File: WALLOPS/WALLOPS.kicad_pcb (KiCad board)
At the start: 2 copper layers, 55 x 67 mm, 19 parts, among them J1 JST-PH 1x8 Connector - WALLOP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, Q1 AO3401A, U1 VL53L8CX 0 (Zwicky), U2 VL58L8CX 1 (Aristotle), U3 VL53L8CX 3 (Copernicus), U4 VL53L8CX 2 (Brahe), U5 6DOF IMU (Sisko), U6 5V to 3.3V Converter

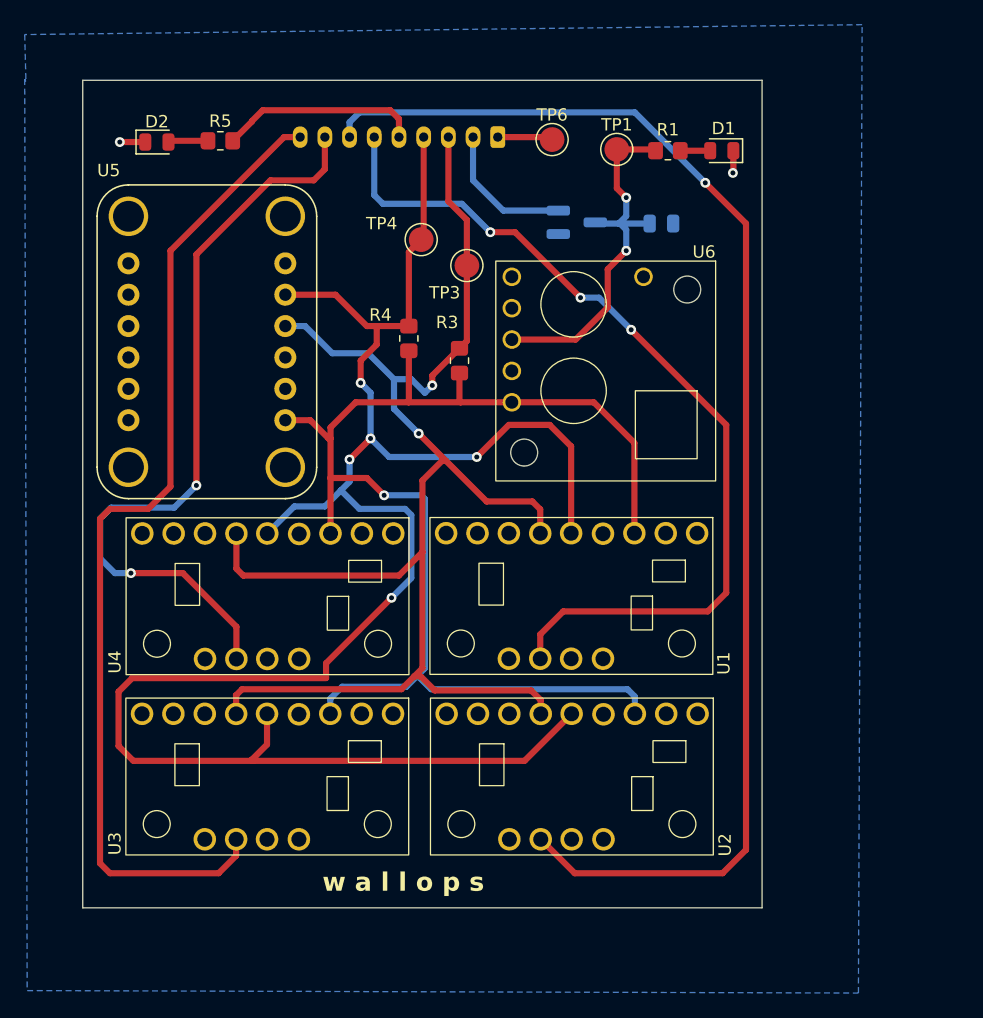
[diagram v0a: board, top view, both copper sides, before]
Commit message: Reduced size in WALLOPS
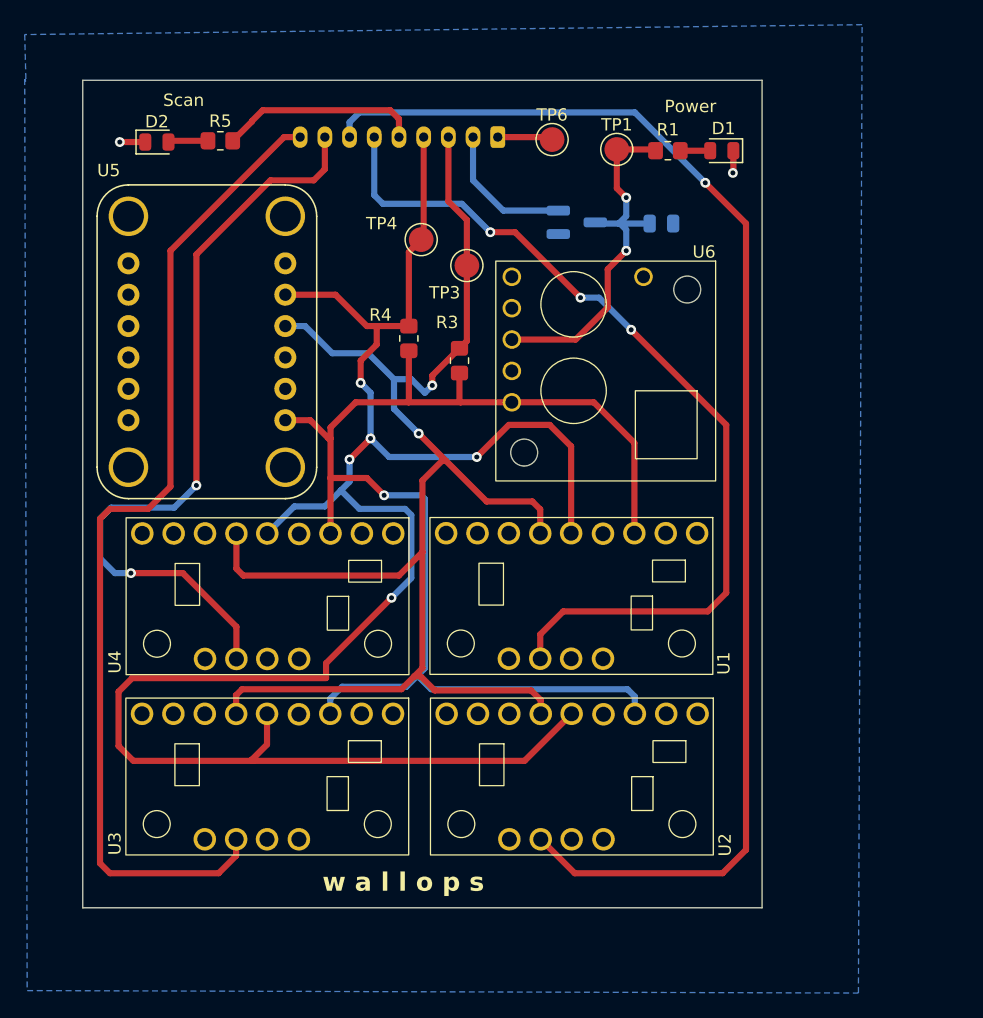
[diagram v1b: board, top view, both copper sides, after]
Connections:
- J1 pad 2: /5Vin -> /5VinML
- Q1 pad 2: /5Vin -> /5VinML
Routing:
- net /5Vin: track 42.2 -> 30.7 mm
- net /5VinML: track 0.00 -> 11.4 mm
- net /SDA: track 163.1 -> 162.5 mm
- net GND: track 8.93 -> 8.36 mm
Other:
- board text added: "Power"
- board text added: "Scan"
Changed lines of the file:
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@@
 	(net 36 "unconnected-(U6-EN-Pad2)")
 	(net 37 "unconnected-(U6-VOUT-Pad6)")
+	(net 38 "/5VinML")
 	(footprint "RockSat:VL53L8CX"
 		(layer "F.Cu")
@@
 			(layers "B.Cu" "B.Mask" "B.Paste")
 			(roundrect_rratio 0.25)
-			(net 1 "/5Vin")
+			(net 38 "/5VinML")
 			(pinfunction "S")
 			(pintype "passive")
@@
 			(layers "*.Cu" "*.Mask")
 			(remove_unused_layers no)
-			(net 1 "/5Vin")
+			(net 38 "/5VinML")
 			(pinfunction "Pin_2")
 			(pintype "passive")
@@
 		(layer "Edge.Cuts")
 	)
+	(gr_text "Scan"
+		(at 166.5 40.2 0)
+		(layer "F.SilkS")
+		(effects
+			(font
+				(size 1 1)
+				(thickness 0.15)
+			)
+			(justify left bottom)
+		)
+	)
+	(gr_text "Power"
+		(at 207.1 40.7 0)
+		(layer "F.SilkS")
+		(effects
+			(font
+				(size 1 1)
+				(thickness 0.15)
+			)
+			(justify left bottom)
+		)
+	)
 	(gr_text "w a l l o p s"
 		(at 179.4 103.8 0)
@@
 	)
 	(segment
-		(start 191.6 42.6)
-		(end 191.6 46.1)
-		(width 0.5)
-		(layer "B.Cu")
-		(net 1)
-	)
-	(segment
-		(start 204 51.8)
-		(end 204 51.9)
-		(width 0.5)
-		(layer "B.Cu")
-		(net 1)
-	)
-	(segment
-		(start 191.6 46.1)
-		(end 194.05 48.55)
-		(width 0.5)
-		(layer "B.Cu")
-		(net 1)
-	)
-	(segment
 		(start 204 50.1)
 		(end 204 51.8)
@@
 	)
 	(segment
-		(start 194.05 48.55)
-		(end 198.5 48.55)
-		(width 0.5)
-		(layer "B.Cu")
-		(net 1)
-	)
-	(segment
 		(start 201.5 49.5)
 		(end 201.7 49.5)
@@
 		(net 2)
 	)
-	(segment
-		(start 198.2 42.6)
-		(end 198.6 43)
-		(width 0.5)
-		(layer "F.Cu")
-		(net 2)
-	)
 	(via
 		(at 163 43)
@@
 	)
 	(segment
-		(start 175.4 89.77)
-		(end 174.92 89.29)
-		(width 0.5)
-		(layer "F.Cu")
-		(net 6)
-	)
-	(segment
 		(start 186.4 57.9)
 		(end 183.8 57.9)
@@
 	)
 	(segment
-		(start 163.9 77.9)
-		(end 164 77.9)
-		(width 0.5)
-		(layer "B.Cu")
-		(net 9)
-	)
-	(segment
 		(start 162.6 77.9)
 		(end 163.9 77.9)
@@
 		(net 12)
 	)
+	(segment
+		(start 191.6 42.6)
+		(end 191.6 46.1)
+		(width 0.5)
+		(layer "B.Cu")
+		(net 38)
+	)
+	(segment
+		(start 191.6 46.1)
+		(end 194.05 48.55)
+		(width 0.5)
+		(layer "B.Cu")
+		(net 38)
+	)
+	(segment
+		(start 194.05 48.55)
+		(end 198.5 48.55)
+		(width 0.5)
+		(layer "B.Cu")
+		(net 38)
+	)
 	(zone

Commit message: Updated PCB
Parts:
- removed R5: 330Ω, Resistor_SMD:R_0805_2012Metric_Pad1.20x1.40mm_HandSolder
- removed TP6: GND_TP, RockSat:TestPoint_Pad_D2.0mm_With_Tolerance
- added R2: 2.2kΩ, Resistor_SMD:R_0805_2012Metric_Pad1.20x1.40mm_HandSolder, F.Cu at (185.6, 64.7)
- added TP2: 5Vin_Test, RockSat:TestPoint_Pad_D2.0mm_With_Tolerance, F.Cu at (183.9, 59.9)
- J1: value JST-PH 1x8 Connector - WALLOPS to ML Suite -> JST-PH 1x9 Connector - WALLOPS to ML Suite; footprint Connector_JST:JST_PH_B9B-PH-K_1x09_P2.00mm_Vertical -> Connector_JST:JST_PH_S9B-PH-K_1x09_P2.00mm_Horizontal; moved to F.Cu
- R4: value 2.2kΩ -> 330Ω
- TP1: value 5Vin_Test -> GND_TP
- moved D1 44.7 mm to (167.1, 40.8)
- moved R1 44.7 mm to (162.7, 40.8)
- moved U5 34.8 mm to (204.1, 51.6)
- moved TP1 32.7 mm to (170.9, 48.7)
- moved Q1 28.6 mm to (171.7, 53.4), turned to -90 degrees
- moved C1 28.3 mm to (180.2, 59.2), turned to 90 degrees
- moved R4 27.8 mm to (162.8, 44.3), turned to 0 degrees
- moved J1 27.4 mm to (166.8, 48.7), turned to -90 degrees
- moved U6 23.2 mm to (185.1, 47.1), turned to 0 degrees
- moved TP4 19.1 mm to (175.3, 65.7)
- moved TP3 15.4 mm to (180.9, 64.6)
- moved R3 15.3 mm to (177.7, 69.0), turned to 180 degrees
- moved D2 1.89 mm to (167.3, 44.4), turned to 180 degrees
- moved U2 0.99 mm to (199.7, 93.4)
- moved U3 0.99 mm to (175.0, 93.4)
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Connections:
- R3 pad 1: /SCL -> /3.3VOUT
- R3 pad 2: /3.3VOUT -> /SDA
- R4 pad 1: /3.3VOUT -> /SCAN_LED
- R4 pad 2: /SDA -> Net-(D2-A)
- TP1 pad 1: /5Vin -> GND
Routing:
- net /SDA: track 162.5 -> 18.8 mm, vias 5 -> 0
- net /LPn_1: track 106.6 -> 0.00 mm, vias 1 -> 0
- net /LPn_3: track 81.4 -> 0.00 mm
- net /LPn_0: track 72.9 -> 0.00 mm, vias 3 -> 0
- net /LPn_2: track 62.6 -> 0.00 mm, vias 2 -> 0
- net /3.3VOUT: track 105.2 -> 64.2 mm, vias 1 -> 0
- net /SCL: track 122.2 -> 91.5 mm, vias 2 -> 3
- net /5Vin: track 30.7 -> 53.9 mm, vias 2 -> 3
- net /5VinML: track 11.4 -> 9.35 mm, vias 0 -> 1
- net GND: track 8.36 -> 9.71 mm, vias 2 -> 3
- net /SCAN_LED: track 16.3 -> 15.4 mm
- net Net-(D2-A): track 3.24 -> 2.57 mm
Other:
- outline, holes or cut-outs redrawn

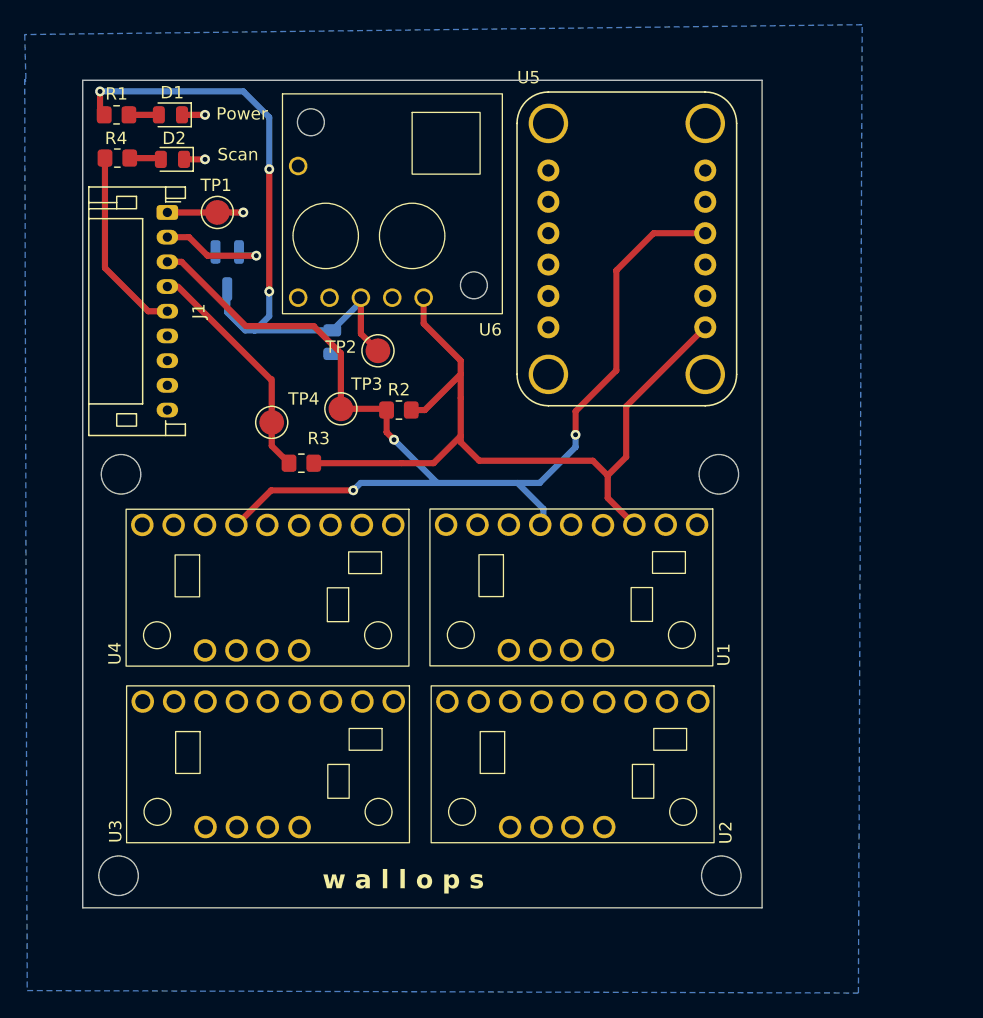
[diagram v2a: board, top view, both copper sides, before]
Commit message: Reduced size of PCB
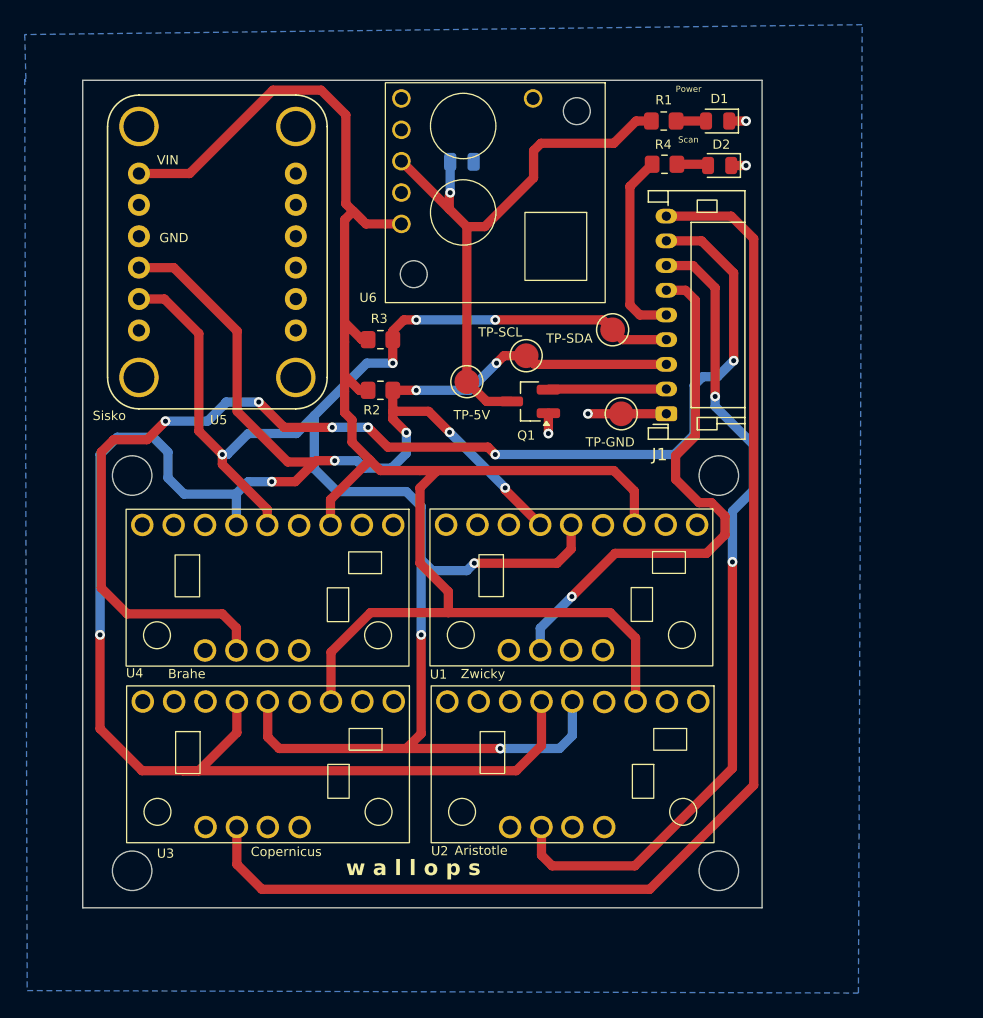
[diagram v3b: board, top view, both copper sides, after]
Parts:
- Q1: moved to F.Cu
- moved D1 44.3 mm to (211.4, 41.3)
- moved D2 44.3 mm to (211.6, 44.9)
- moved R1 44.3 mm to (207.0, 41.3)
- moved R4 44.3 mm to (207.1, 44.8)
- moved J1 43.6 mm to (207.2, 65.0), turned to 90 degrees
- moved TP-GND 36.5 mm to (203.6, 65.0), turned to -90 degrees
- moved U5 33.2 mm to (170.9, 51.9), turned to -90 degrees
- moved TP-SDA 28.6 mm to (202.9, 58.2), turned to 180 degrees
- moved Q1 26.7 mm to (196.2, 64.0), turned to 180 degrees
- moved C1 18.0 mm to (190.7, 44.6), turned to 180 degrees
- moved TP-SCL 15.6 mm to (195.9, 60.3), turned to 180 degrees
- moved R3 11.9 mm to (184.1, 59.0), turned to 0 degrees
- moved U6 9.23 mm to (194.3, 47.1), turned to -90 degrees
- moved TP-5V 7.62 mm to (191.1, 62.4), turned to 180 degrees
- moved R2 2.19 mm to (184.1, 63.1), turned to 180 degrees
- renumbered TP2 to TP-5V, TP1 to TP-GND, TP3 to TP-SCL, TP4 to TP-SDA
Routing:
- net /SDA: track 18.8 -> 147.1 mm, vias 0 -> 7
- net /LPn_3: track 0.00 -> 101.3 mm
- net /LPn_2: track 0.00 -> 98.9 mm, vias 0 -> 6
- net /SCL: track 91.5 -> 174.3 mm, vias 3 -> 8
- net /3.3VOUT: track 64.2 -> 143.6 mm
- net /LPn_1: track 0.00 -> 67.0 mm, vias 0 -> 2
- net /LPn_0: track 0.00 -> 44.5 mm, vias 0 -> 1
- net /5Vin: track 53.9 -> 48.0 mm, vias 3 -> 1
- net GND: track 9.71 -> 10.6 mm, vias 3 -> 4
- net /5VinML: track 9.35 -> 9.57 mm, vias 1 -> 0
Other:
- outline, holes or cut-outs redrawn
- board text added: "Aristotle"
- board text added: "Brahe"
- board text added: "Copernicus"
- board text added: "GND"
- board text added: "Sisko"
- board text added: "VIN"
- board text added: "Zwicky"

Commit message: Added silkscreen to WALLOPS pcb
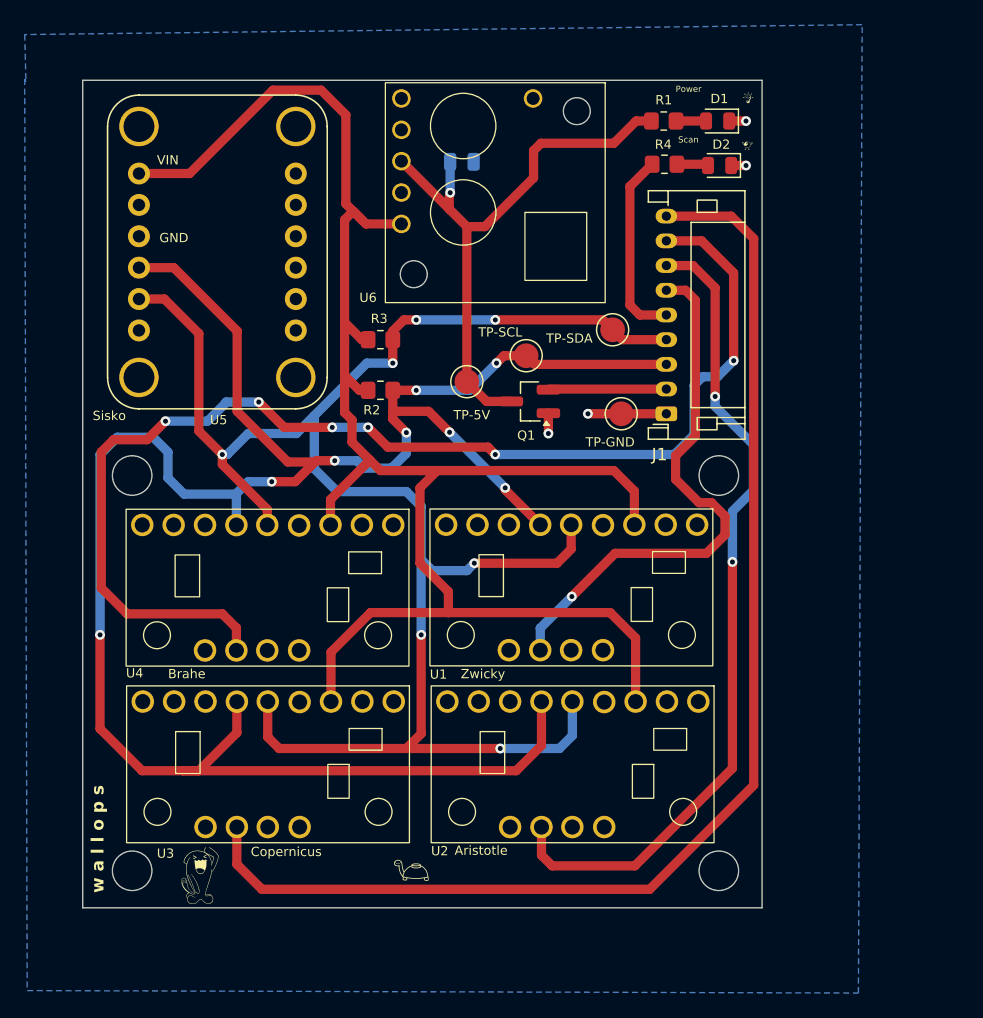
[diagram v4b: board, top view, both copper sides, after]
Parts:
- added G***: LOGO, LOGO, F.Cu at (213.9, 39.4)
- added G***: LOGO, LOGO, F.Cu at (213.8, 43.3)
- added G***: LOGO, LOGO, F.Cu at (186.7, 102.0)
- added G***: LOGO, LOGO, F.Cu at (169.5, 102.4)
- added G***: LOGO, LOGO, B.Cu at (171.0, 51.4)
- added G***: LOGO, LOGO, B.Cu at (186.1, 97.2)

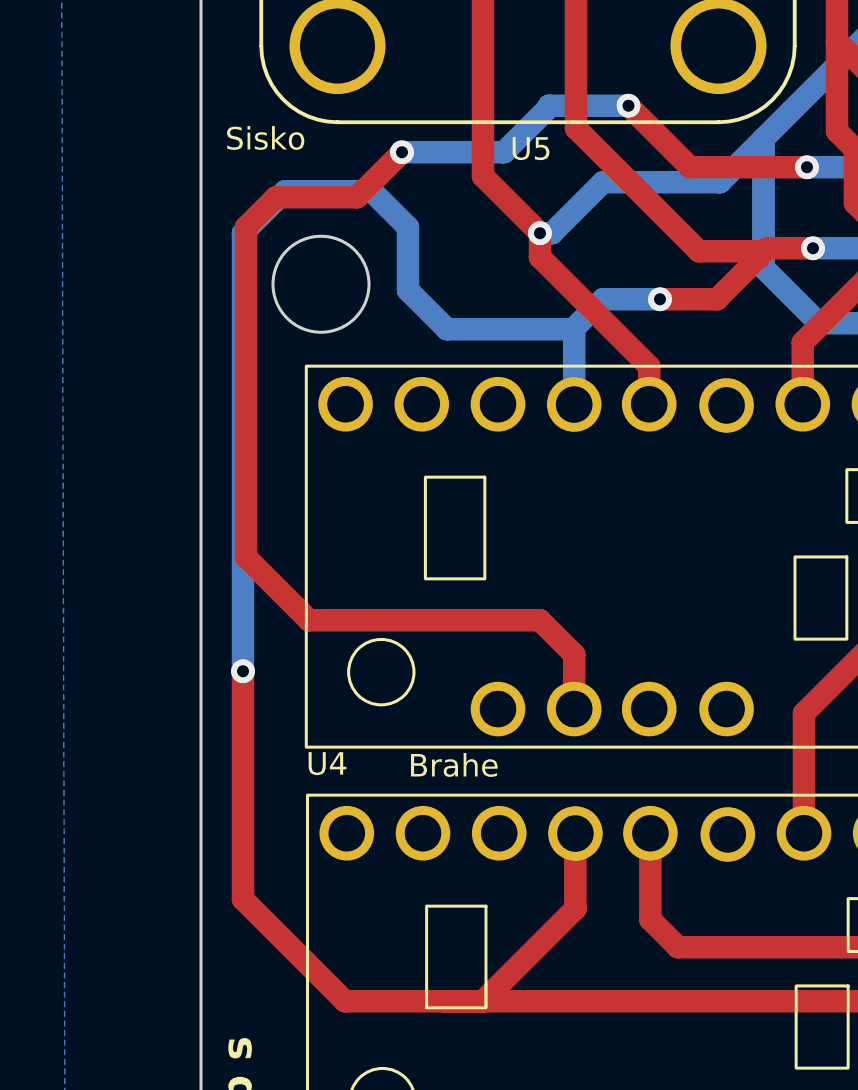
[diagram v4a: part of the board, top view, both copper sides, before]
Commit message: Added teardrops to WALLOPS LiDAR PCB
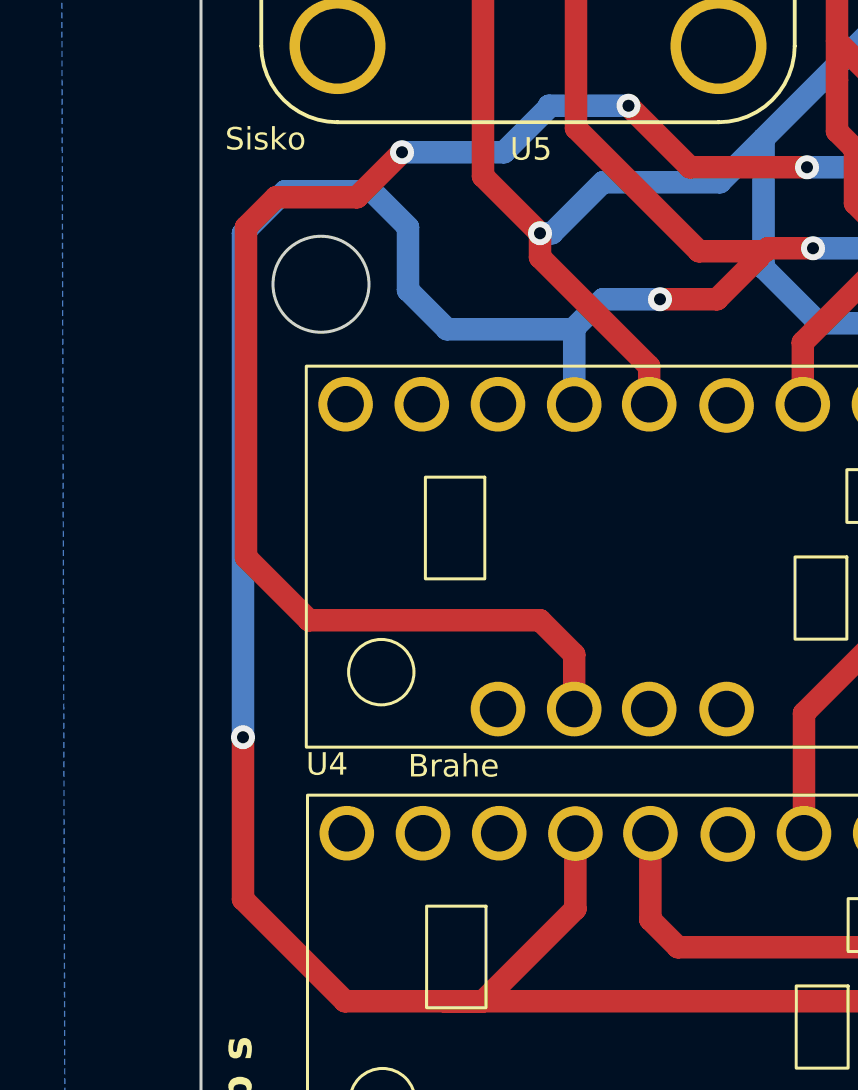
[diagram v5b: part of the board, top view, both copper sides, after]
